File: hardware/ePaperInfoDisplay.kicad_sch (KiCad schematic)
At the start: 52 parts, among them J1 Conn_01x02_Pin, J2 USB_C_Receptacle_USB2.0, Q1 Q_NMOS_GSD, Q2 Q_PMOS_GSD, Q3 Q_PMOS_GSD, SW1 SW_Push, SW2 SW_Push, U1 MCP73831-2-OT, U2 MIC5219-3.3YM5, U3 ePD_iTC

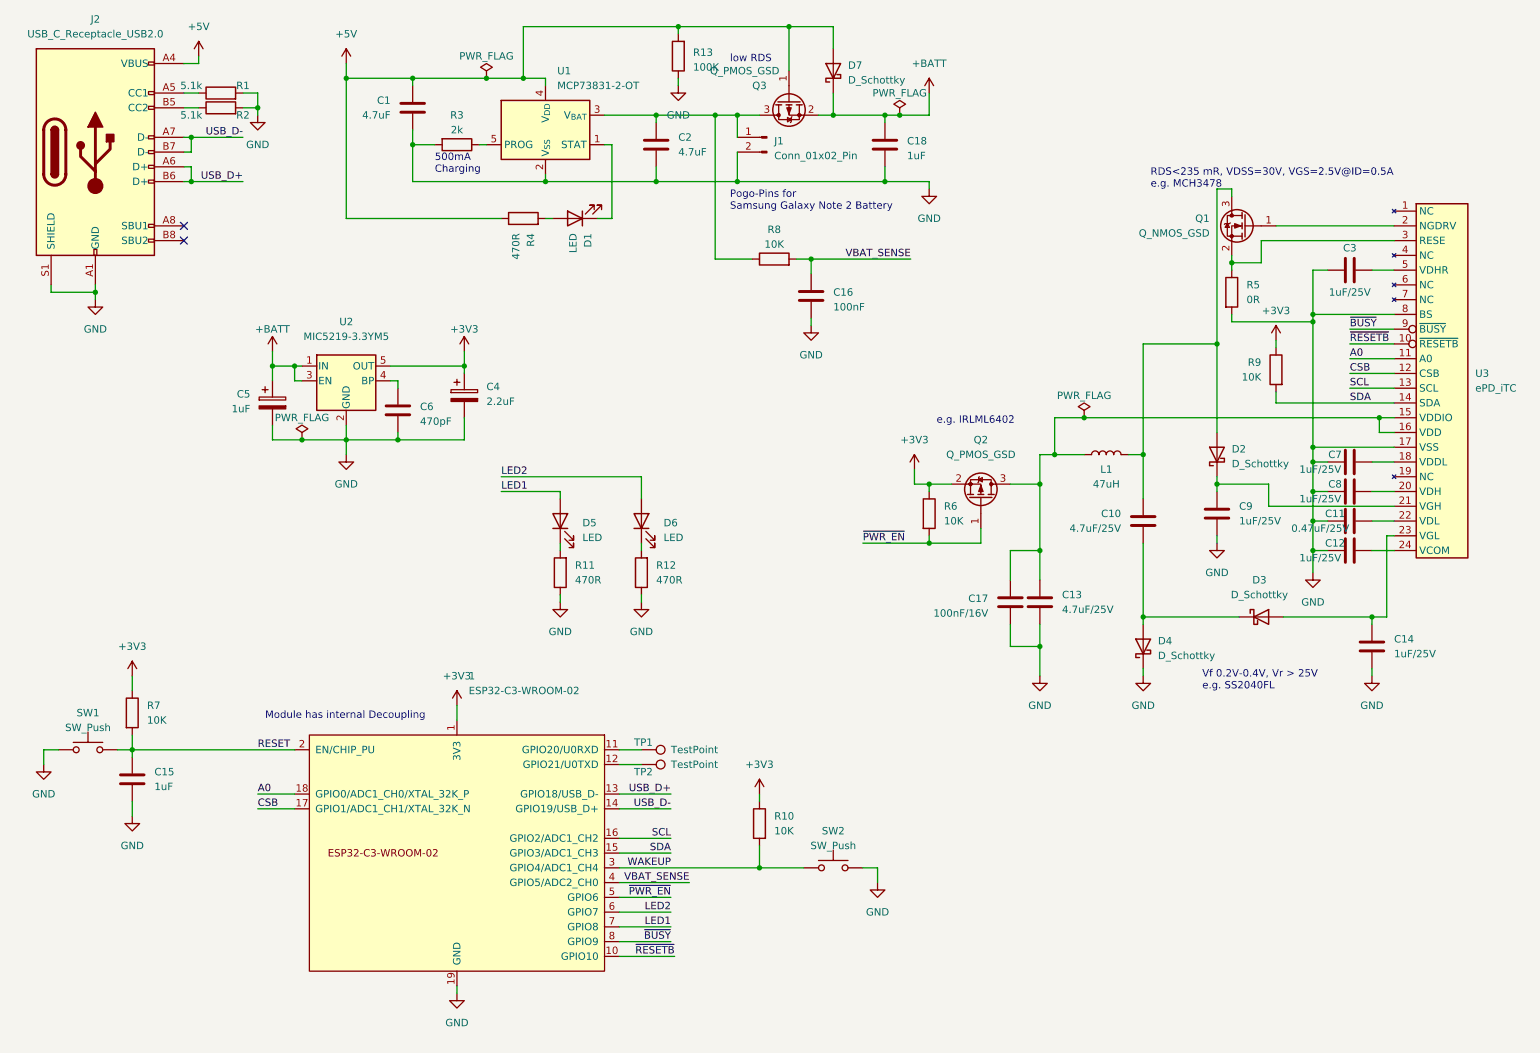
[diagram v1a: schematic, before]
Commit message: Update hardware to Rev. 3
Fixed all of the known issues:
- Fixed swapped USB DP+/-, USB usable again
- Fixed swapped labels USR1/USR2
- Add resistor divider for VBAT_SENSE to avoid excessive voltage on GPIO pin
- WAKEUP button changed to BOOT (connected to GPIO9)
- VBAT_SENSE moved to GPIO4 which has a usable ADC
- GPIO association of some signals changed to avoid issues strapping pins:
	- LED1 now on GPIO5
	- LED2 now on GPIO6
	- /BUSY now on GPIO7
	- /PWR_EN now on GPIO8
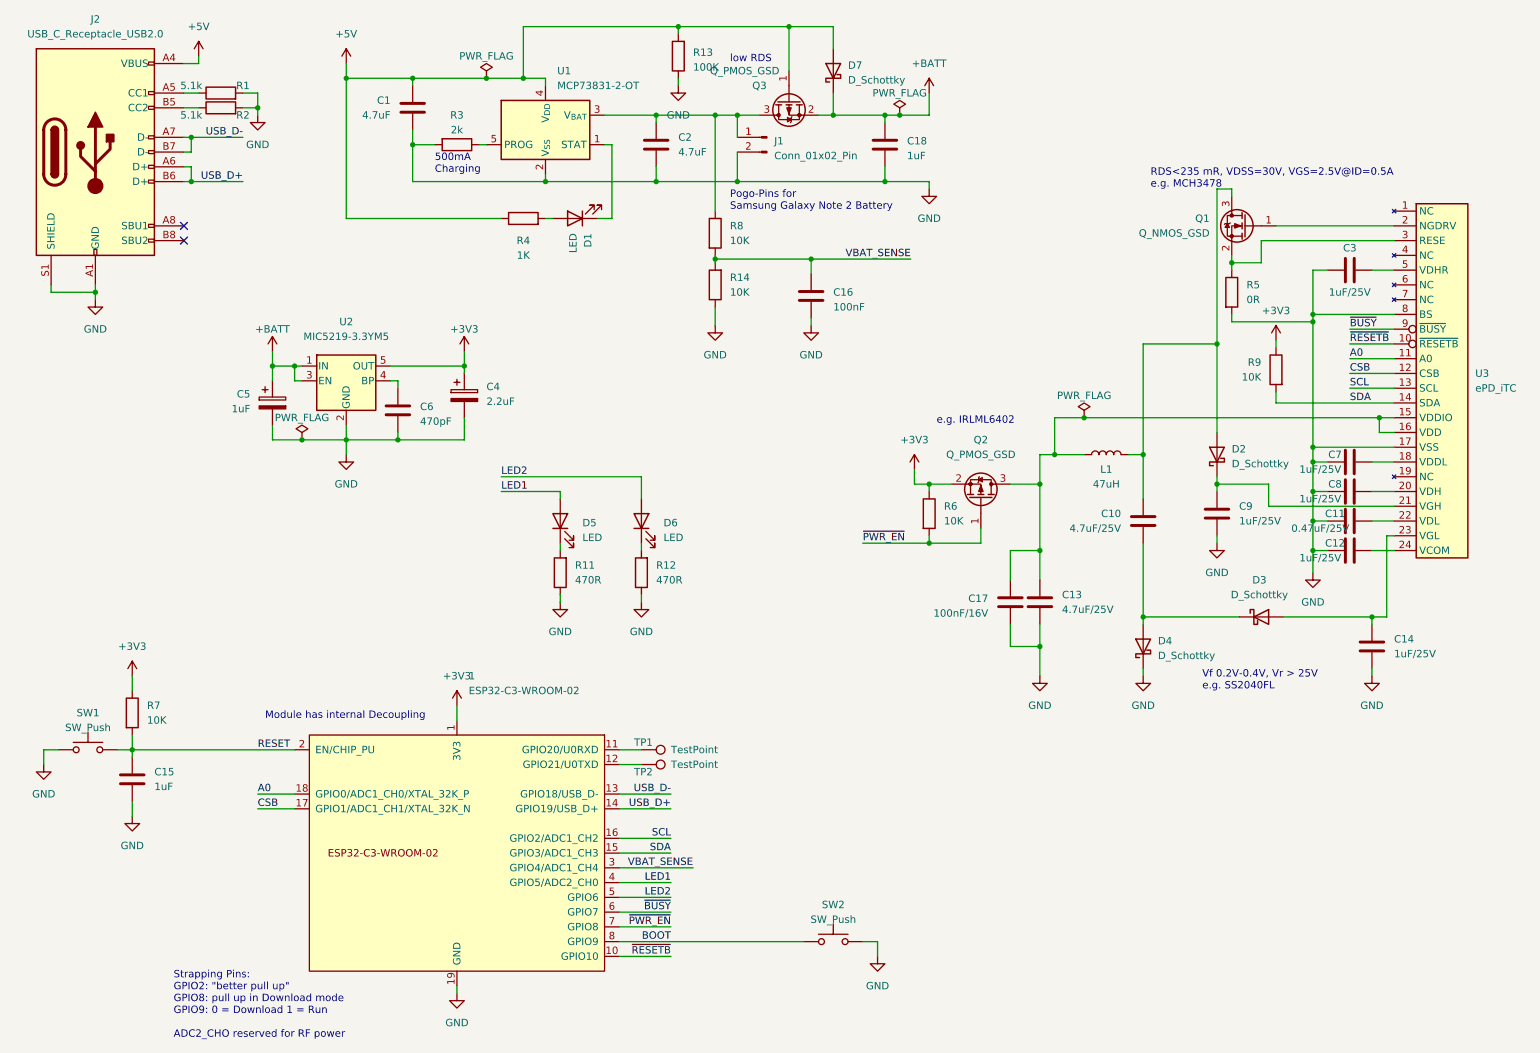
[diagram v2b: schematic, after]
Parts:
- removed R10: 10K, Resistor_SMD:R_0805_2012Metric_Pad1.20x1.40mm_HandSolder, symbol Device:R
- added R14: 10K, Resistor_SMD:R_0805_2012Metric_Pad1.20x1.40mm_HandSolder, symbol Device:R
- R4: value 470R -> 1K
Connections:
- net GND: now also R14.1
- net LED1: now also 1.4 (GPIO5/ADC2_CH0); no longer 1.7 (GPIO8)
- net LED2: now also 1.5 (GPIO6); no longer 1.6 (GPIO7)
- net USB_D+: now also 1.14 (GPIO19/USB_D+); no longer 1.13 (GPIO18/USB_D-)
- net USB_D-: now also 1.13 (GPIO18/USB_D-); no longer 1.14 (GPIO19/USB_D+)
- net VBAT_SENSE: now also 1.3 (GPIO4/ADC1_CH4), R14.2; no longer 1.4 (GPIO5/ADC2_CH0)
- net ~{BUSY}: now also 1.6 (GPIO7); no longer 1.8 (GPIO9)
- net ~{PWR_EN}: now also 1.7 (GPIO8); no longer 1.5 (GPIO6)
- net WAKEUP renamed BOOT
- net BOOT: now also 1.8 (GPIO9); no longer 1.3 (GPIO4/ADC1_CH4)
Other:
- note added: "Strapping Pins: GPIO2: "better pull up" GPIO8: pull up in Download mode GPIO9: 0 = Download 1 = Run ADC2_CHO reserved for RF power"
- moved on the sheet: R8, SW2
